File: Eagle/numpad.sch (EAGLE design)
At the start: 19 parts, among them SW1 SWITCH-SMD-SCHURTER-1241.1612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, U1 PROMICRO

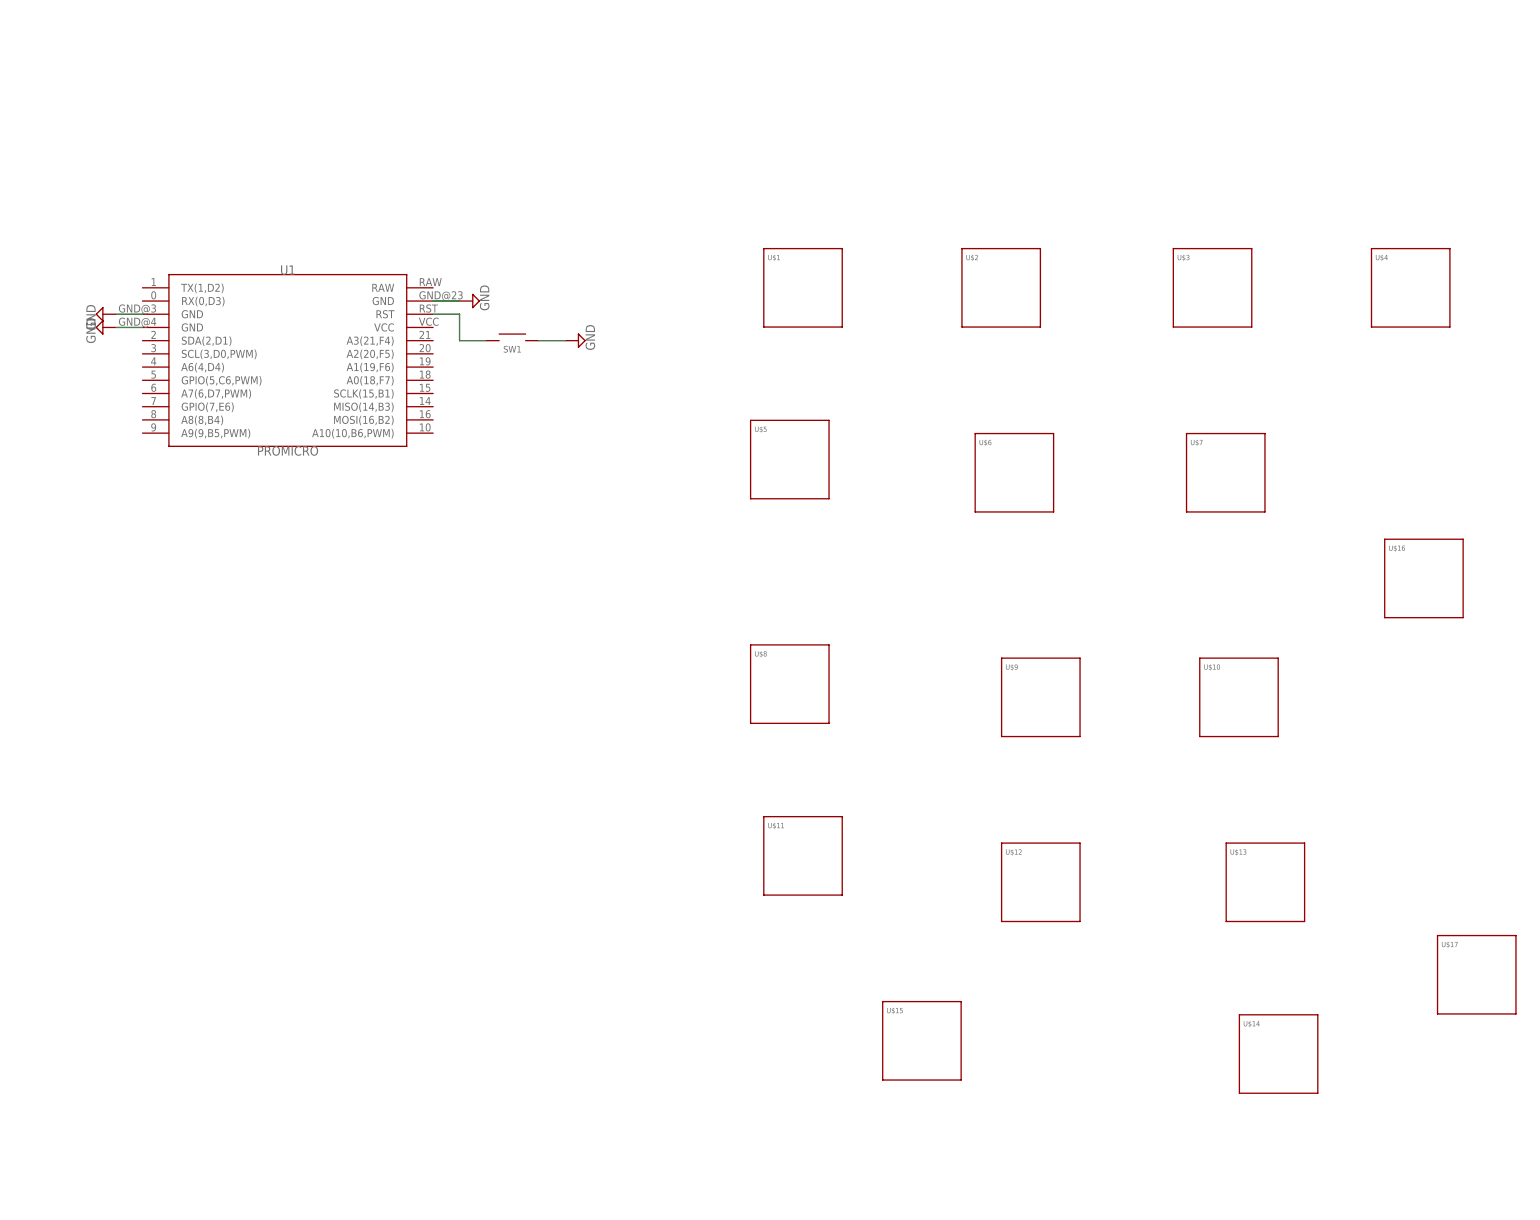
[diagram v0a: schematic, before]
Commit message: moved files due to eagle error
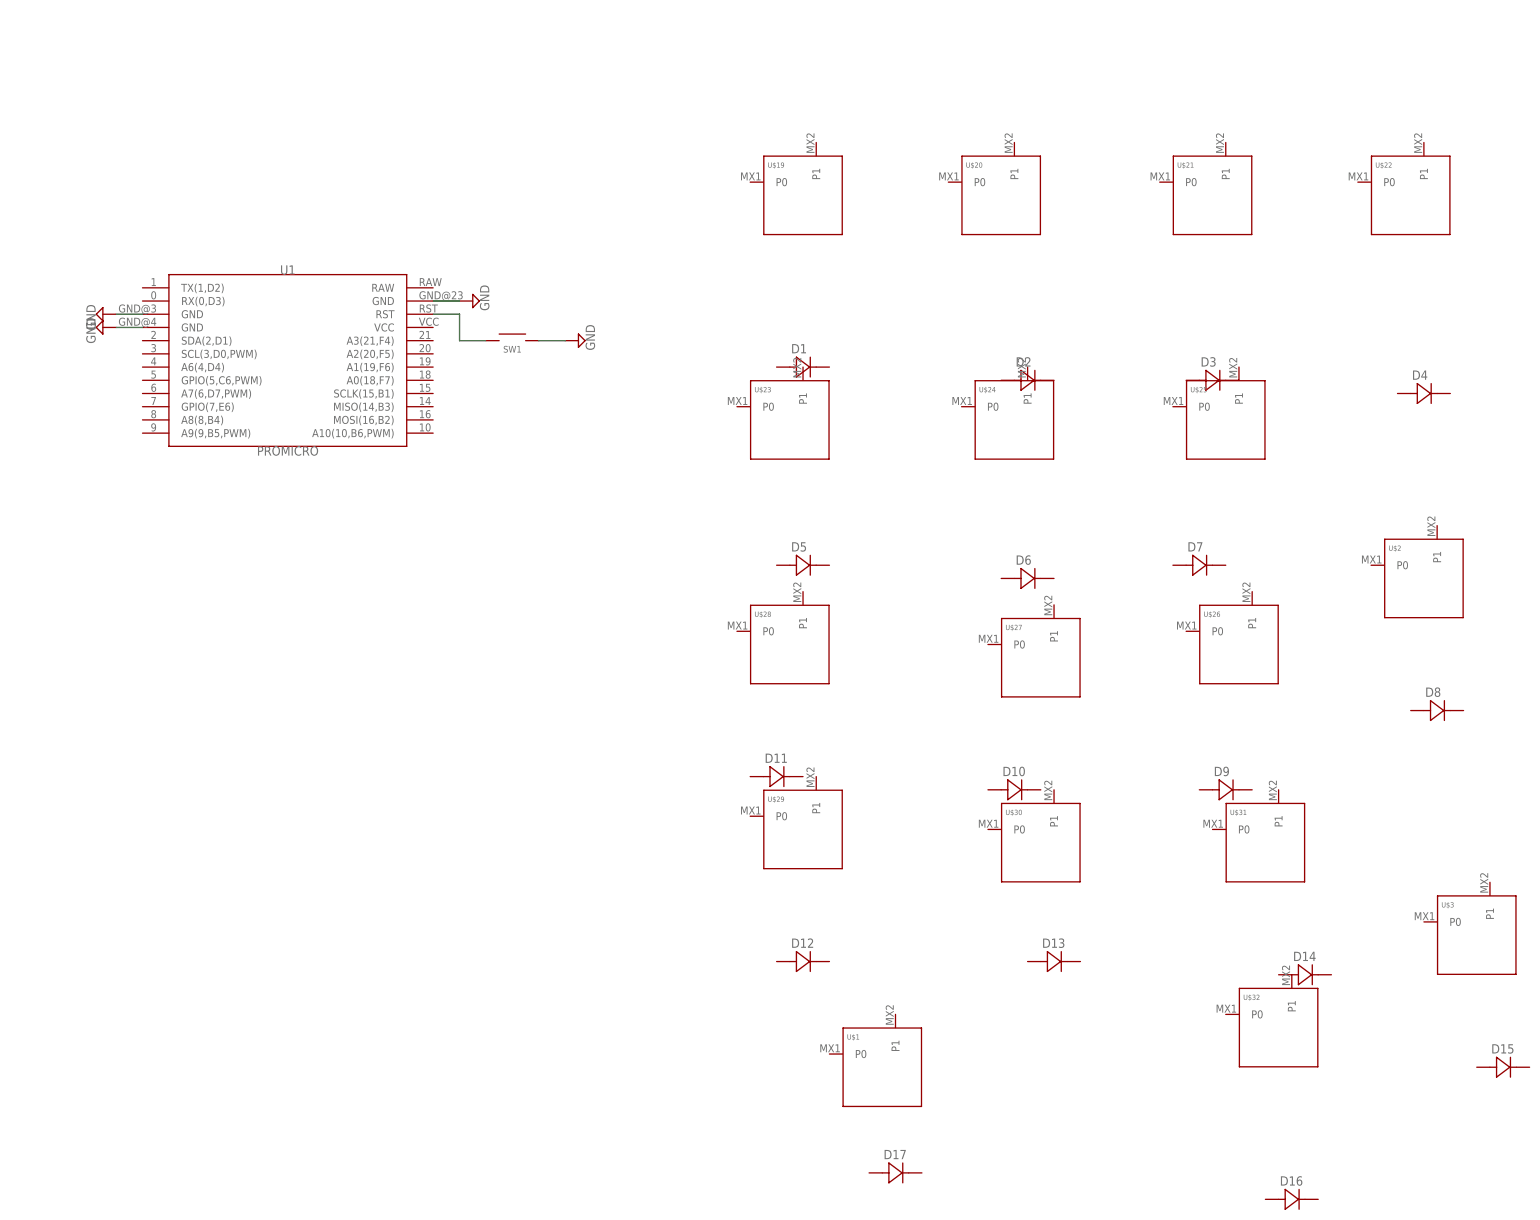
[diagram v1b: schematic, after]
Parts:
- removed U$10, U$11, U$12, U$13, U$14, U$4, U$5, U$6, U$7, U$8, U$9: KEYSWITCH-PLATE-MXPLATE-1U, Keyboard:KEYSWITCH-PLATE-MXPLATE-1U
- removed U$15: KEYSWITCH-PLATE-MXPLATE-2U, Keyboard:KEYSWITCH-PLATE-MXPLATE-2U
- removed U$16, U$17: KEYSWITCH-PLATE-MXPLATE-2U-ROTATED, Keyboard:KEYSWITCH-PLATE-MXPLATE-2U-ROTATED
- added D1, D10, D11, D12, D13, D14, D15, D16, D17, D2, D3, D4, D5, D6, D7, D8, D9: (no value), Components:DIODE-HAND
- added U$19, U$20, U$21, U$22, U$23, U$24, U$25, U$26, U$27, U$28, U$29, U$30, U$31, U$32: KEYSWITCH-PLAIN-MX-1U, Keyboard:KEYSWITCH-PLAIN-MX-1U
- U$1: value KEYSWITCH-PLATE-MXPLATE-1U -> KEYSWITCH-PLAIN-MX-2U; device Keyboard:KEYSWITCH-PLATE-MXPLATE-1U -> Keyboard:KEYSWITCH-PLAIN-MX-2U
- U$2, U$3: value KEYSWITCH-PLATE-MXPLATE-1U -> KEYSWITCH-PLAIN-MX-2U-ROTATED; device Keyboard:KEYSWITCH-PLATE-MXPLATE-1U -> Keyboard:KEYSWITCH-PLAIN-MX-2U-ROTATED

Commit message: finished first test of board, need to finish placement of switches
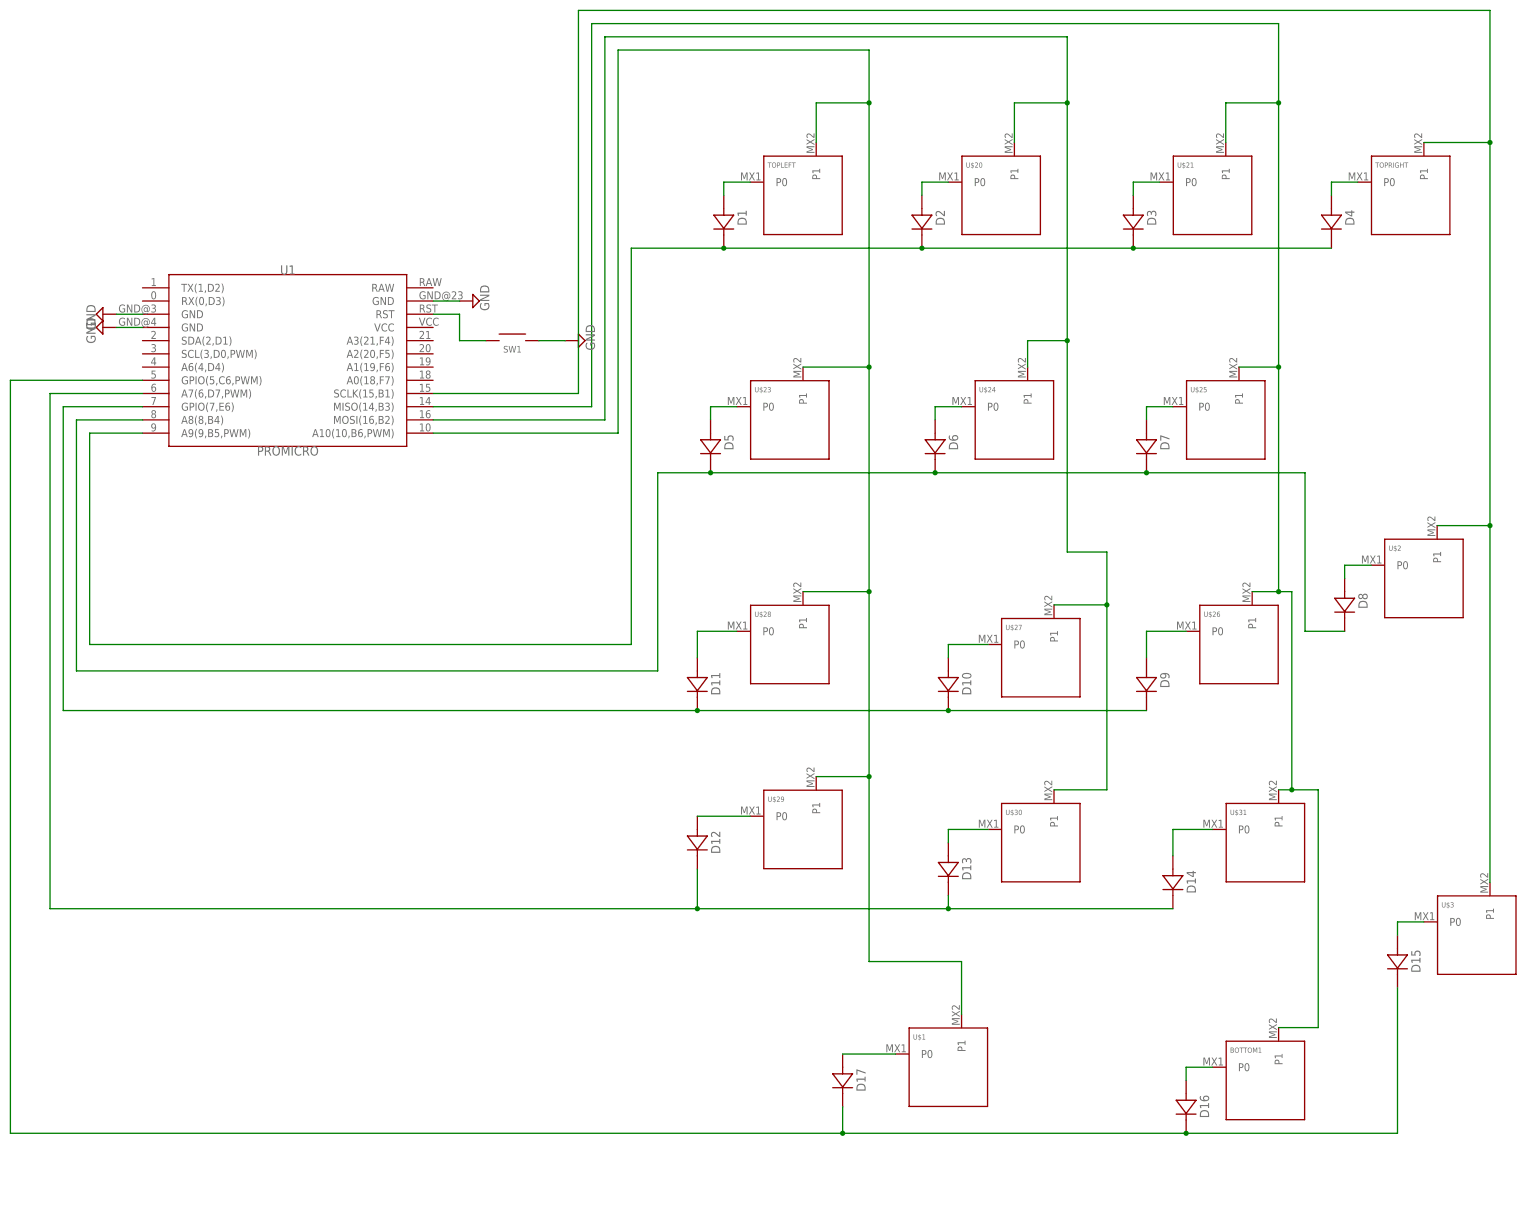
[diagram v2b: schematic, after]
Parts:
- removed U$32: KEYSWITCH-PLAIN-MX-1U, Keyboard:KEYSWITCH-PLAIN-MX-1U
- added BOTTOM1: KEYSWITCH-PLAIN-MX-1U, Keyboard:KEYSWITCH-PLAIN-MX-1U
- U$1: value KEYSWITCH-PLAIN-MX-2U -> KEYSWITCH-PLAIN-MX-2U-FLIPPED; device Keyboard:KEYSWITCH-PLAIN-MX-2U -> Keyboard:KEYSWITCH-PLAIN-MX-2U-FLIPPED
- renumbered U$19 to TOPLEFT, U$22 to TOPRIGHT
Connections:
- new net N$10: D6.A, U$24.P0
- new net N$11: D7.A, U$25.P0
- new net N$12: D8.A, U$2.P0
- new net N$13: D9.A, U$26.P0
- new net N$14: D10.A, U$27.P0
- new net N$15: D11.A, U$28.P0
- new net N$16: D12.A, U$29.P0
- new net N$17: D13.A, U$30.P0
- new net N$18: D14.A, U$31.P0
- new net N$19: BOTTOM1.P0, D16.A
- new net N$2: D1.A, TOPLEFT.P0
- new net N$20: D17.A, U$1.P0
- new net N$21: D15.A, U$3.P0
- new net N$22: D15.C, D16.C, D17.C, U1.GPIO(5,C6,PWM)
- new net N$23: D12.C, D13.C, D14.C, U1.A7(6,D7,PWM)
- new net N$24: D10.C, D11.C, D9.C, U1.GPIO(7,E6)
- new net N$26: D5.C, D6.C, D7.C, D8.C, U1.A8(8,B4)
- new net N$27: BOTTOM1.P1, U$21.P1, U$25.P1, U$26.P1, U$31.P1, U1.MISO(14,B3)
- new net N$3: D2.A, U$20.P0
- new net N$30: TOPRIGHT.P1, U$2.P1, U$3.P1, U1.SCLK(15,B1)
- new net N$4: D3.A, U$21.P0
- new net N$5: D4.A, TOPRIGHT.P0
- new net N$6: D1.C, D2.C, D3.C, D4.C, U1.A9(9,B5,PWM)
- new net N$7: TOPLEFT.P1, U$1.P1, U$23.P1, U$28.P1, U$29.P1, U1.A10(10,B6,PWM)
- new net N$8: D5.A, U$23.P0
- new net N$9: U$20.P1, U$24.P1, U$27.P1, U$30.P1, U1.MOSI(16,B2)
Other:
- moved on the sheet: D1, D10, D11, D12, D13, D14, D15, D16, D17, D2, D3, D4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

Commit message: added hole
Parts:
- D1, D10, D11, D12, D13, D14, D15, D16, D17, D2, D3, D4, D5, D6, D7, D8, D9: value (none) -> 1N4148; device Components:DIODE-HAND -> Components:DIODE-DO-35
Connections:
- net N$27 renamed COL2
- net N$30 renamed COL3
- net N$6 renamed ROW0
- net N$7 renamed COL0
- net N$9 renamed COL1
- removed net N$16: D12.A, U$29.P0
- removed net N$22: D15.C, D16.C, D17.C, U1.GPIO(5,C6,PWM)
- removed net N$23: D12.C, D13.C, D14.C, U1.A7(6,D7,PWM)
- removed net N$24: D10.C, D11.C, D9.C, U1.GPIO(7,E6)
- removed net N$26: D5.C, D6.C, D7.C, D8.C, U1.A8(8,B4)
- new net N$6: D15.A, U$29.P0
- new net ROW1: D5.C, D6.C, D7.C, U1.A8(8,B4)
- new net ROW2: D10.C, D11.C, D8.C, D9.C, U1.GPIO(7,E6)
- new net ROW3: D13.C, D14.C, D15.C, U1.A7(6,D7,PWM)
- new net ROW4: D12.C, D16.C, D17.C, U1.GPIO(5,C6,PWM)
- net N$12: now also D11.A; no longer D8.A
- net N$13: now also D10.A; no longer D9.A
- net N$14: now also D9.A; no longer D10.A
- net N$15: now also D8.A; no longer D11.A
- net N$17: now also D14.A; no longer D13.A
- net N$18: now also D13.A; no longer D14.A
- net N$21: now also D12.A; no longer D15.A
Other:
- moved on the sheet: D10, D11, D12, D13, D14, D15, D8, D9, U$29

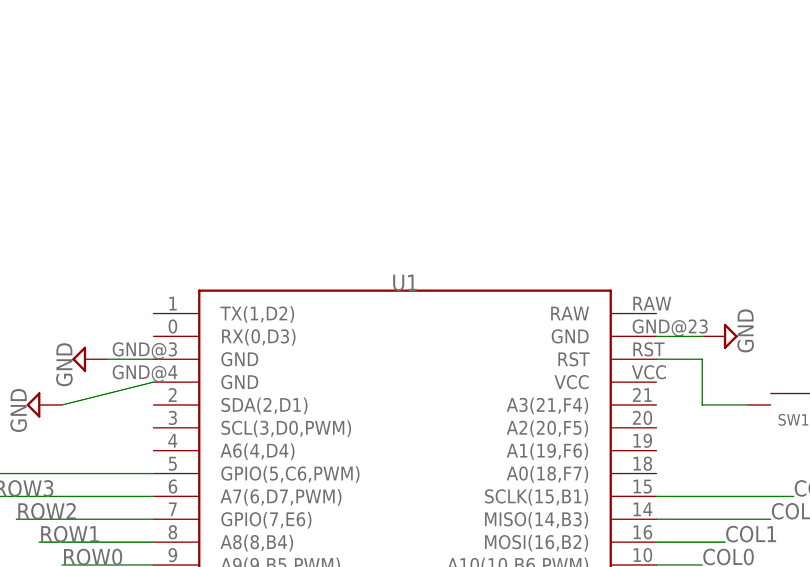
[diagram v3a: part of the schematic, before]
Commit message: replaced promicro and relayed wire
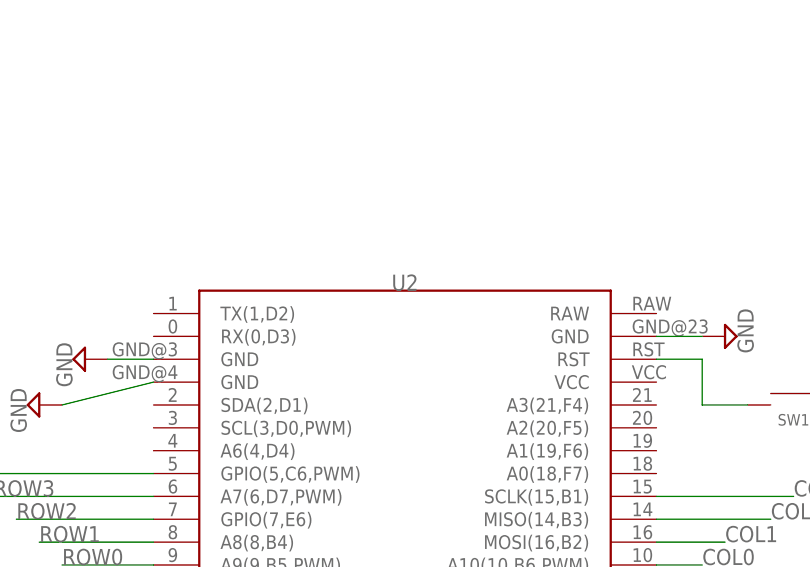
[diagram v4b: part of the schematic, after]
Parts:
- renumbered U1 to U2
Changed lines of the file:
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@@
 </classes>
 <parts>
-<part name="U1" library="MCU" deviceset="PROMICRO" device=""/>
 <part name="SUPPLY1" library="supply2" library_urn="urn:adsk.eagle:library:372" deviceset="GND" device=""/>
 <part name="SUPPLY2" library="supply2" library_urn="urn:adsk.eagle:library:372" deviceset="GND" device=""/>
@@
 <part name="D17" library="Components" deviceset="DIODE" device="-DO-35" value="1N4148"/>
 <part name="D1" library="Components" deviceset="DIODE" device="-DO-35" value="1N4148"/>
+<part name="U2" library="MCU" deviceset="PROMICRO" device=""/>
 </parts>
 <sheets>
@@
 </plain>
 <instances>
-<instance part="U1" gate="G$1" x="73.66" y="25.4" smashed="yes">
-<attribute name="NAME" x="73.66" y="40.64" size="1.778" layer="95" align="bottom-center"/>
-<attribute name="VALUE" x="73.66" y="7.62" size="1.778" layer="96" align="top-center"/>
-</instance>
 <instance part="SUPPLY1" gate="GND" x="109.22" y="35.56" smashed="yes" rot="R90">
 <attribute name="VALUE" x="112.395" y="33.655" size="1.778" layer="96" rot="R90"/>
@@
 <attribute name="NAME" x="160.1216" y="53.1114" size="1.778" layer="95" rot="R270"/>
 <attribute name="VALUE" x="152.9842" y="53.3654" size="1.778" layer="96" rot="R270"/>
+</instance>
+<instance part="U2" gate="G$1" x="73.66" y="25.4" smashed="yes">
+<attribute name="NAME" x="73.66" y="40.64" size="1.778" layer="95" align="bottom-center"/>
+<attribute name="VALUE" x="73.66" y="7.62" size="1.778" layer="96" align="top-center"/>
 </instance>
 </instances>
@@
 <pinref part="SUPPLY3" gate="GND" pin="GND"/>
 <pinref part="SUPPLY2" gate="GND" pin="GND"/>
-<pinref part="U1" gate="G$1" pin="GND@3"/>
 <wire x1="45.72" y1="33.02" x2="40.64" y2="33.02" width="0.1524" layer="91"/>
-<pinref part="U1" gate="G$1" pin="GND@4"/>
 <wire x1="45.72" y1="30.48" x2="35.56" y2="27.94" width="0.1524" layer="91"/>
-</segment>
-<segment>
-<pinref part="U1" gate="G$1" pin="GND@23"/>
+<pinref part="U2" gate="G$1" pin="GND@4"/>
+<pinref part="U2" gate="G$1" pin="GND@3"/>
+</segment>
+<segment>
 <pinref part="SUPPLY1" gate="GND" pin="GND"/>
 <wire x1="101.6" y1="35.56" x2="106.68" y2="35.56" width="0.1524" layer="91"/>
+<pinref part="U2" gate="G$1" pin="GND@23"/>
 </segment>
 <segment>
@@
 <wire x1="111.76" y1="27.94" x2="106.68" y2="27.94" width="0.1524" layer="91"/>
 <wire x1="106.68" y1="27.94" x2="106.68" y2="33.02" width="0.1524" layer="91"/>
-<pinref part="U1" gate="G$1" pin="RST"/>
 <wire x1="106.68" y1="33.02" x2="101.6" y2="33.02" width="0.1524" layer="91"/>
+<pinref part="U2" gate="G$1" pin="RST"/>
 </segment>
 </net>
@@
 <net name="ROW4" class="0">
 <segment>
-<pinref part="U1" gate="G$1" pin="GPIO(5,C6,PWM)"/>
 <wire x1="20.32" y1="20.32" x2="45.72" y2="20.32" width="0.1524" layer="91"/>
 <label x="20.32" y="20.32" size="1.778" layer="95"/>
+<pinref part="U2" gate="G$1" pin="GPIO(5,C6,PWM)"/>
 </segment>
 <segment>
@@
 <net name="ROW3" class="0">
 <segment>
-<pinref part="U1" gate="G$1" pin="A7(6,D7,PWM)"/>
 <wire x1="27.94" y1="17.78" x2="45.72" y2="17.78" width="0.1524" layer="91"/>
 <label x="27.94" y="17.78" size="1.778" layer="95"/>
+<pinref part="U2" gate="G$1" pin="A7(6,D7,PWM)"/>
 </segment>
 <segment>
@@
 <net name="ROW1" class="0">
 <segment>
-<pinref part="U1" gate="G$1" pin="A8(8,B4)"/>
 <wire x1="45.72" y1="12.7" x2="33.02" y2="12.7" width="0.1524" layer="91"/>
 <label x="33.02" y="12.7" size="1.778" layer="95"/>
+<pinref part="U2" gate="G$1" pin="A8(8,B4)"/>
 </segment>
 <segment>
@@
 <net name="ROW2" class="0">
 <segment>
-<pinref part="U1" gate="G$1" pin="GPIO(7,E6)"/>
 <wire x1="30.48" y1="15.24" x2="45.72" y2="15.24" width="0.1524" layer="91"/>
 <label x="30.48" y="15.24" size="1.778" layer="95"/>
+<pinref part="U2" gate="G$1" pin="GPIO(7,E6)"/>
 </segment>
 <segment>
@@
 </segment>
 <segment>
-<pinref part="U1" gate="G$1" pin="A10(10,B6,PWM)"/>
 <wire x1="101.6" y1="10.16" x2="106.68" y2="10.16" width="0.1524" layer="91"/>
 <label x="106.68" y="10.16" size="1.778" layer="95"/>
+<pinref part="U2" gate="G$1" pin="A10(10,B6,PWM)"/>
 </segment>
 </net>
@@
 </segment>
 <segment>
-<pinref part="U1" gate="G$1" pin="MISO(14,B3)"/>
 <wire x1="101.6" y1="15.24" x2="114.3" y2="15.24" width="0.1524" layer="91"/>
 <label x="114.3" y="15.24" size="1.778" layer="95"/>
+<pinref part="U2" gate="G$1" pin="MISO(14,B3)"/>
 </segment>
 </net>
@@
 </segment>
 <segment>
-<pinref part="U1" gate="G$1" pin="MOSI(16,B2)"/>
 <wire x1="101.6" y1="12.7" x2="109.22" y2="12.7" width="0.1524" layer="91"/>
 <label x="109.22" y="12.7" size="1.778" layer="95"/>
+<pinref part="U2" gate="G$1" pin="MOSI(16,B2)"/>
 </segment>
 </net>
@@
 </segment>
 <segment>
-<pinref part="U1" gate="G$1" pin="SCLK(15,B1)"/>
 <wire x1="101.6" y1="17.78" x2="116.84" y2="17.78" width="0.1524" layer="91"/>
 <label x="116.84" y="17.78" size="1.778" layer="95"/>
+<pinref part="U2" gate="G$1" pin="SCLK(15,B1)"/>
 </segment>
 </net>
@@
 </segment>
 <segment>
-<pinref part="U1" gate="G$1" pin="A9(9,B5,PWM)"/>
 <wire x1="45.72" y1="10.16" x2="35.56" y2="10.16" width="0.1524" layer="91"/>
 <label x="35.56" y="10.16" size="1.778" layer="95"/>
-</segment>
-</net>
+<pinref part="U2" gate="G$1" pin="A9(9,B5,PWM)"/>
+</segment>
+</net>
